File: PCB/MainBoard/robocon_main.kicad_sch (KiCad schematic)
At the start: 21 parts, among them J1 MOTOR_OUT, J10 Conn_01x03_Pin, J11 to_SERVO, J2 POWER, J3 MOTOR_OUT, J4 to_COLOR, J5 MOTOR_OUT, J7 MOTOR_OUT, J9 to_CAM, SW1 POW, U1 OKL-T/6-W12N-C, U2 RP2040, U3 TB67H450, U4 3-Terminal Regulator, U5 TB67H450, U6 TB67H450, U7 TB67H450, U8 BNO055

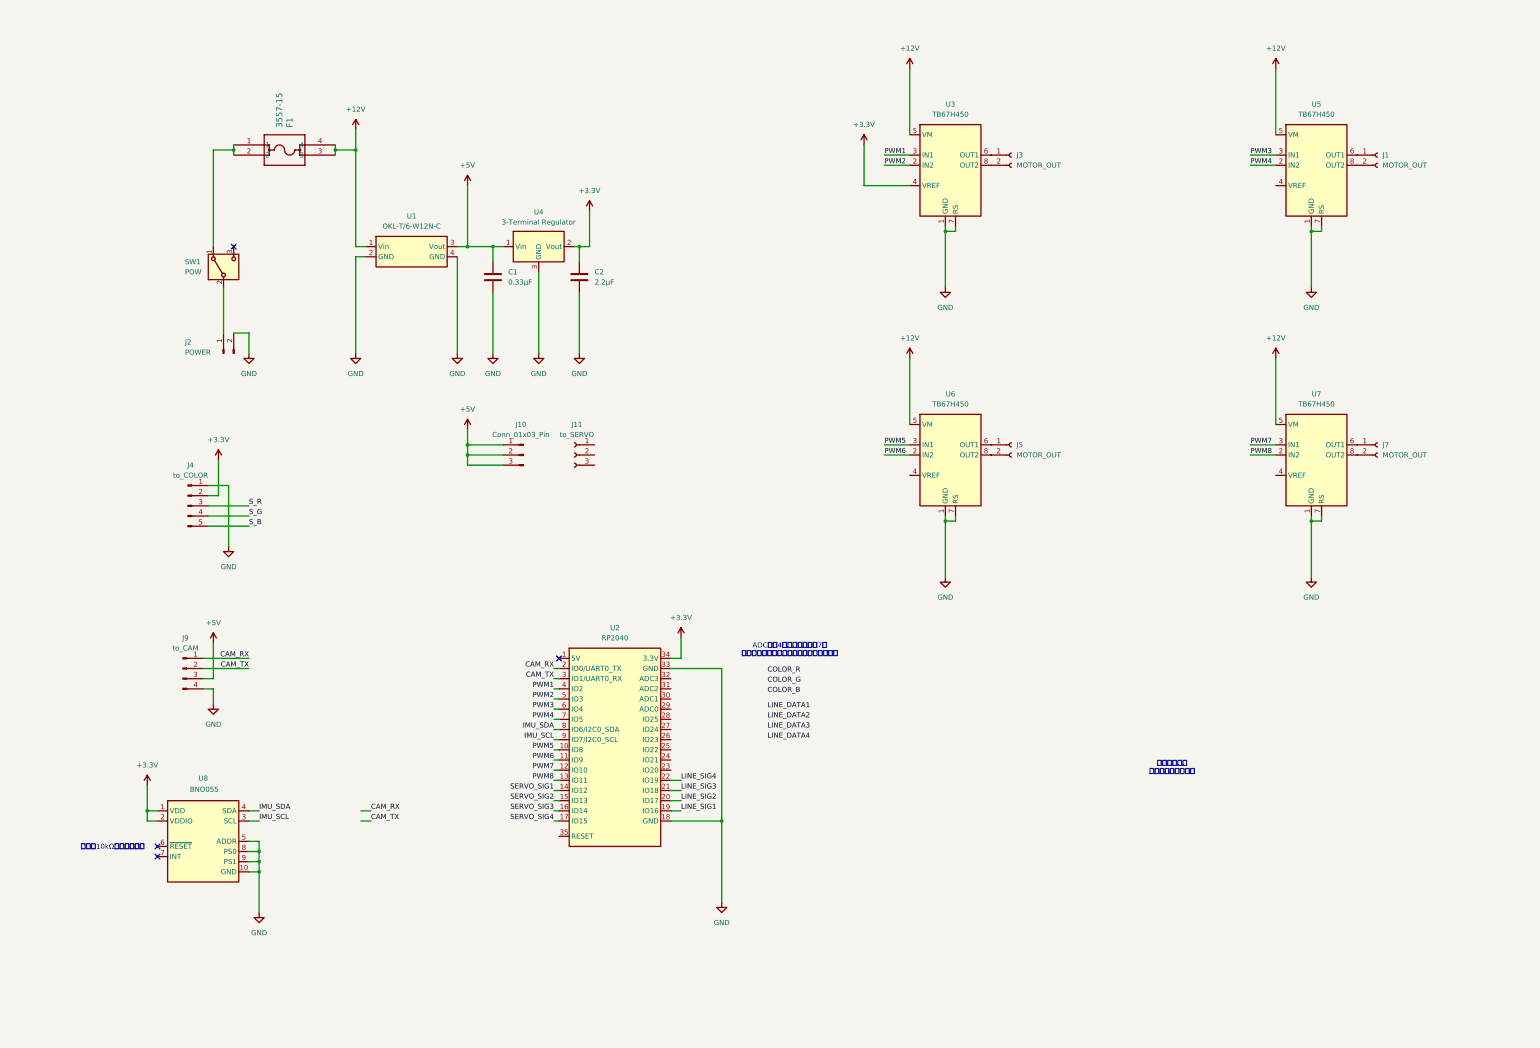
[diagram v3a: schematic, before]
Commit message: サーボ、ラインセンサのコネクタ化、ラベル更新
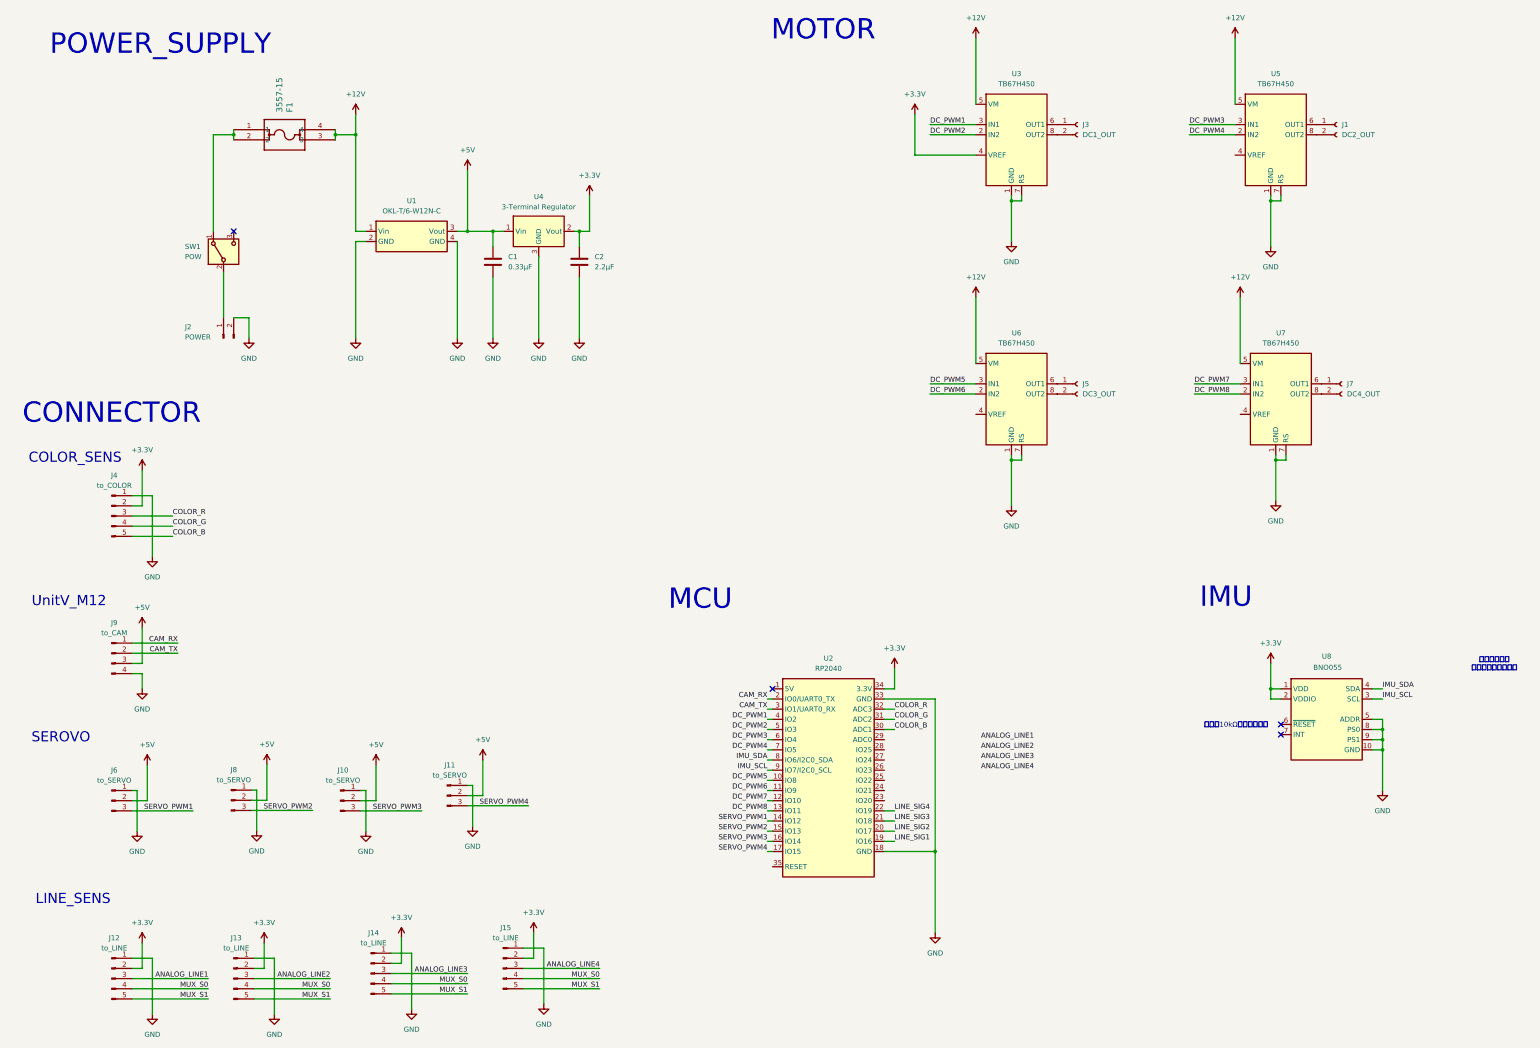
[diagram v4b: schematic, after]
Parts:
- removed J11: to_SERVO, symbol Connector:Conn_01x03_Socket
- added J11, J6, J8: to_SERVO, symbol Connector:Conn_01x03_Pin
- added J12, J13, J14, J15: to_LINE, symbol Connector:Conn_01x05_Pin
- J1: value MOTOR_OUT -> DC2_OUT
- J10: value Conn_01x03_Pin -> to_SERVO
- J3: value MOTOR_OUT -> DC1_OUT
- J5: value MOTOR_OUT -> DC3_OUT
- J7: value MOTOR_OUT -> DC4_OUT
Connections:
- net S_B is gone; now on net COLOR_B: J4.5 (Pin_5)
- net S_G is gone; now on net COLOR_G: J4.4 (Pin_4)
- net S_R is gone; now on net COLOR_R: J4.3 (Pin_3)
- net +3.3V: now also J12.2 (Pin_2), J13.2 (Pin_2), J14.2 (Pin_2), J15.2 (Pin_2)
- net +5V: now also J11.2 (Pin_2), J6.2 (Pin_2), J8.2 (Pin_2); no longer J10.1 (Pin_1), J10.3 (Pin_3)
- net COLOR_B: now also U2.30 (ADC1)
- net COLOR_G: now also U2.31 (ADC2)
- net COLOR_R: now also U2.32 (ADC3)
- net GND: now also J10.1 (Pin_1), J11.1 (Pin_1), J12.1 (Pin_1), J13.1 (Pin_1), J14.1 (Pin_1), J15.1 (Pin_1), J6.1 (Pin_1), J8.1 (Pin_1)
- net PWM1 renamed DC_PWM1
- net PWM2 renamed DC_PWM2
- net PWM3 renamed DC_PWM3
- net PWM4 renamed DC_PWM4
- net PWM5 renamed DC_PWM5
- net PWM6 renamed DC_PWM6
- net PWM7 renamed DC_PWM7
- net PWM8 renamed DC_PWM8
- net SERVO_SIG1 renamed SERVO_PWM1
- net SERVO_PWM1: now also J6.3 (Pin_3)
- net SERVO_SIG2 renamed SERVO_PWM2
- net SERVO_PWM2: now also J8.3 (Pin_3)
- net SERVO_SIG3 renamed SERVO_PWM3
- net SERVO_PWM3: now also J10.3 (Pin_3)
- net SERVO_SIG4 renamed SERVO_PWM4
- net SERVO_PWM4: now also J11.3 (Pin_3)
- new net ANALOG_LINE1: J12.3 (Pin_3)
- new net ANALOG_LINE2: J13.3 (Pin_3)
- new net ANALOG_LINE3: J14.3 (Pin_3)
- new net ANALOG_LINE4: J15.3 (Pin_3)
- new net MUX_S0: J12.4 (Pin_4), J13.4 (Pin_4), J14.4 (Pin_4), J15.4 (Pin_4)
- new net MUX_S1: J12.5 (Pin_5), J13.5 (Pin_5), J14.5 (Pin_5), J15.5 (Pin_5)
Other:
- note added: "COLOR_SENS"
- note added: "CONNECTOR"
- note added: "IMU"
- note added: "LINE_SENS"
- note added: "MCU"
- note added: "MOTOR"
- note added: "POWER_SUPPLY"
- note added: "SEROVO"
- note added: "UnitV_M12"
- note removed: "ADCピン4本に対して信号7本 どのようにつなぐ？（マルチプレクサ？）"
- moved on the sheet: C1, C2, F1, J1, J2, J3, J4, J5, J7, J9, SW1, U1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

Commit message: コネクタ、モタドラの修正 ＆ 電源周りのデバッグIF設計
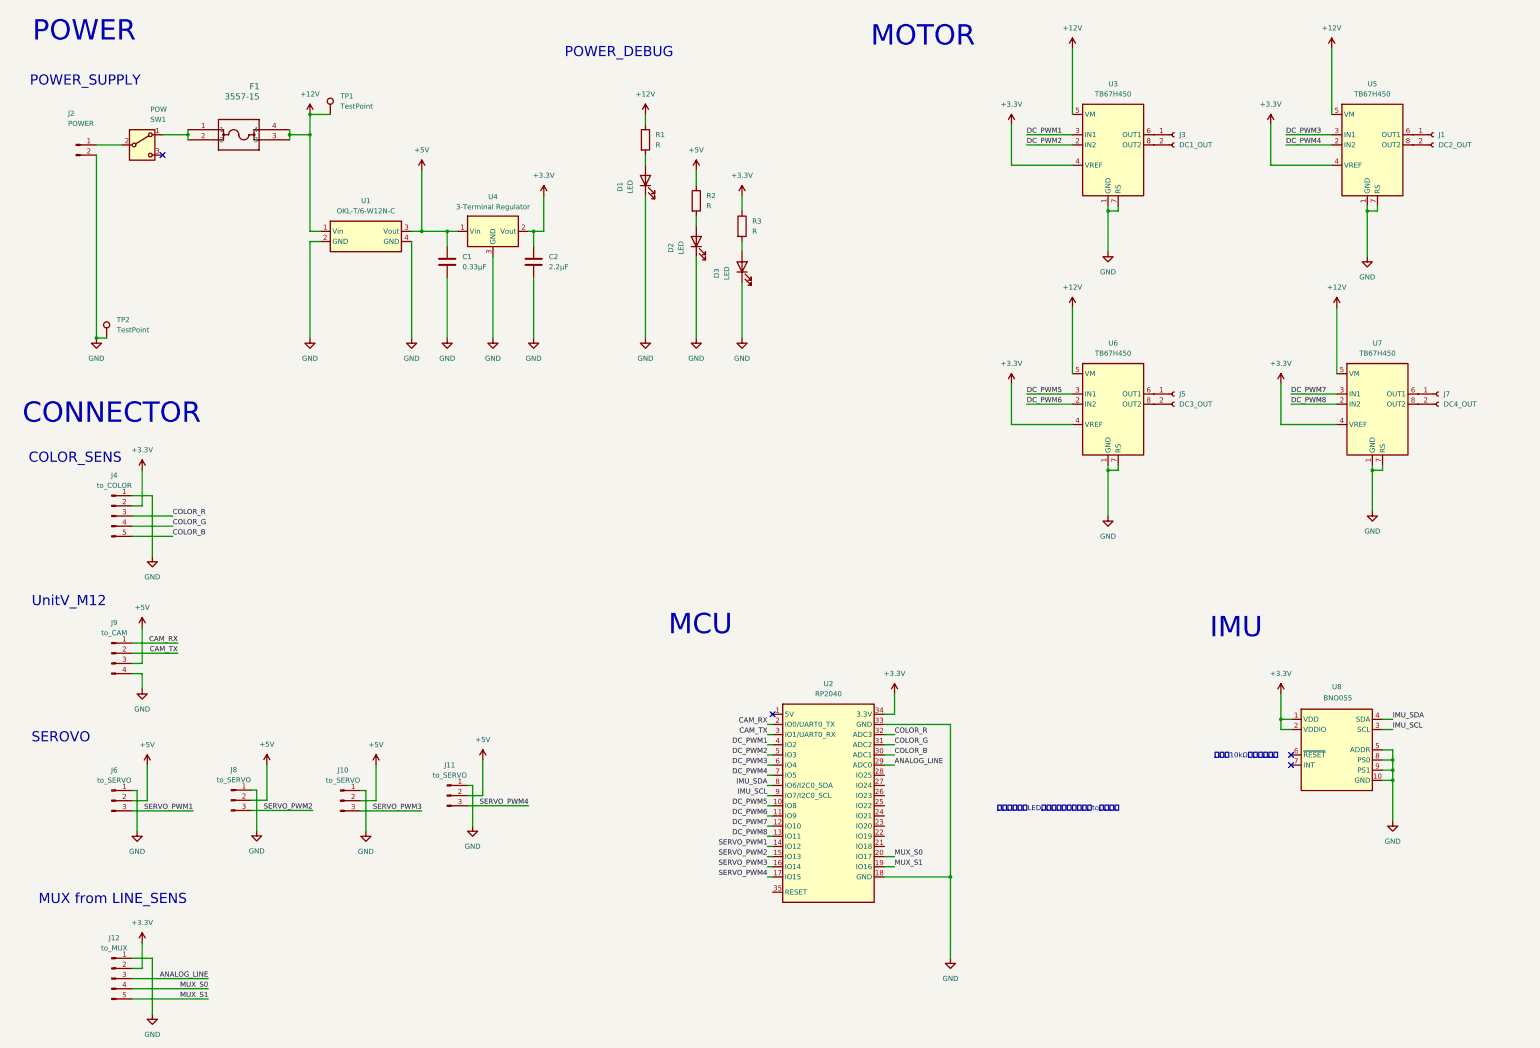
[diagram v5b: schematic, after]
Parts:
- removed J13, J14, J15: to_LINE, symbol Connector:Conn_01x05_Pin
- added D1, D2, D3: LED, symbol Device:LED
- added R1, R2, R3: R, symbol Device:R
- added TP1, TP2: TestPoint, symbol Connector:TestPoint
- J12: value to_LINE -> to_MUX
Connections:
- net ANALOG_LINE1 is gone; now on net ANALOG_LINE: J12.3 (Pin_3)
- net LINE_SIG1 is gone; now on net MUX_S1: U2.19 (IO16)
- net LINE_SIG2 is gone; now on net MUX_S0: U2.20 (IO17)
- net +12V: now also R1.1, TP1.1
- net +3.3V: now also U5.4 (VREF), U6.4 (VREF), U7.4 (VREF), R3.1
- net +5V: now also R2.1
- net GND: now also D1.1 (K), D2.1 (K), D3.1 (K), TP2.1
- net ANALOG_LINE: now reaches U2.29 (ADC0)
- net LINE_SIG3: no longer names the net of U2.21 (IO18)
- net LINE_SIG4: no longer names the net of U2.22 (IO19)
- new net: D2.2 (A), R2.2
- new net: D1.2 (A), R1.2
- new net: D3.2 (A), R3.2
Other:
- note added: "MUX from LINE_SENS"
- note added: "POWER"
- note added: "POWER_DEBUG"
- note added: "デバッグ用のLEDどれくらいほしい？（toソフト）"
- note removed: "LINE_SENS"
- note removed: "サーボのピン バイパスコンデンサ"
- moved on the sheet: C1, C2, F1, J1, J2, J3, J5, J7, SW1, U1, U2, U3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

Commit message: コネクタ追加
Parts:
- added J13: to_MD1, symbol Connector:Conn_01x02_Pin
- added J14: to_MD3, symbol Connector:Conn_01x02_Pin
- added J15: to_MD2, symbol Connector:Conn_01x02_Pin
- added J16: to_MD4, symbol Connector:Conn_01x02_Pin
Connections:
- net DC_PWM1: now also J13.1 (Pin_1)
- net DC_PWM2: now also J13.2 (Pin_2)
- net DC_PWM3: now also J15.1 (Pin_1)
- net DC_PWM4: now also J15.2 (Pin_2)
- net DC_PWM5: now also J14.1 (Pin_1)
- net DC_PWM6: now also J14.2 (Pin_2)
- net DC_PWM7: now also J16.1 (Pin_1)
- net DC_PWM8: now also J16.2 (Pin_2)
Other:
- note added: "MOTOR_DRIVER"

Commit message: フットプリント割り当て_ver.1
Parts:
- F1: footprint 3557-15_KEY -> my_footprints_library:3557-15_KEY
- J10: value to_SERVO -> to_SERVO3; footprint (none) -> Connector_PinHeader_2.54mm:PinHeader_1x03_P2.54mm_Vertical
- J11: value to_SERVO -> to_SERVO4; footprint (none) -> Connector_PinHeader_2.54mm:PinHeader_1x03_P2.54mm_Vertical
- J12: footprint (none) -> Connector_JST:JST_PH_B5B-PH-K_1x05_P2.00mm_Vertical
- J13, J14, J15, J16: footprint (none) -> Connector_JST:JST_XA_B02B-XASK-1-A_1x02_P2.50mm_Vertical
- J2: footprint (none) -> Connector_AMASS:AMASS_XT30U-M_1x02_P5.0mm_Vertical
- J6: value to_SERVO -> to_SERVO1; footprint (none) -> Connector_PinHeader_2.54mm:PinHeader_1x03_P2.54mm_Vertical
- J7: footprint (none) -> Connector_PinHeader_2.54mm:PinHeader_1x03_P2.54mm_Vertical
- J8: value to_SERVO -> to_SERVO2; footprint (none) -> Connector_PinHeader_2.54mm:PinHeader_1x03_P2.54mm_Vertical
- J9: footprint (none) -> Connector:NS-Tech_Grove_1x04_P2mm_Vertical
- TP1, TP2: footprint (none) -> TestPoint:TestPoint_Pad_2.0x2.0mm
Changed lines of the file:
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@@
 			)
 		)
-		(property "Footprint" ""
+		(property "Footprint" "Connector_AMASS:AMASS_XT30U-M_1x02_P5.0mm_Vertical"
 			(at 29.21 49.53 0)
 			(effects
@@
 			)
 		)
-		(property "Footprint" ""
+		(property "Footprint" "Connector_JST:JST_PH_B5B-PH-K_1x05_P2.00mm_Vertical"
 			(at 38.1 257.81 0)
 			(effects
@@
 			)
 		)
-		(property "Footprint" ""
+		(property "Footprint" "Connector_JST:JST_XA_B02B-XASK-1-A_1x02_P2.50mm_Vertical"
 			(at 160.02 134.62 0)
 			(effects
@@
 			)
 		)
-		(property "Value" "to_SERVO"
+		(property "Value" "to_SERVO3"
 			(at 95.885 208.28 0)
 			(effects
@@
 			)
 		)
-		(property "Footprint" ""
+		(property "Footprint" "Connector_PinHeader_2.54mm:PinHeader_1x03_P2.54mm_Vertical"
 			(at 95.25 213.36 0)
 			(effects
@@
 			)
 		)
-		(property "Value" "to_SERVO"
+		(property "Value" "to_SERVO1"
 			(at 38.735 208.28 0)
 			(effects
@@
 			)
 		)
-		(property "Footprint" ""
+		(property "Footprint" "Connector_PinHeader_2.54mm:PinHeader_1x03_P2.54mm_Vertical"
 			(at 38.1 213.36 0)
 			(effects
@@
 			)
 		)
-		(property "Footprint" ""
+		(property "Footprint" "Connector_PinHeader_2.54mm:PinHeader_1x03_P2.54mm_Vertical"
 			(at 369.57 111.76 0)
 			(effects
@@
 			)
 		)
-		(property "Footprint" ""
+		(property "Footprint" "TestPoint:TestPoint_Pad_2.0x2.0mm"
 			(at 87.63 41.91 0)
 			(effects
@@
 			)
 		)
-		(property "Footprint" "3557-15_KEY"
+		(property "Footprint" "my_footprints_library:3557-15_KEY"
 			(at 57.15 45.72 0)
 			(effects
@@
 			)
 		)
-		(property "Footprint" ""
+		(property "Footprint" "TestPoint:TestPoint_Pad_2.0x2.0mm"
 			(at 41.91 97.79 0)
 			(effects
@@
 			)
 		)
-		(property "Footprint" ""
+		(property "Footprint" "Connector_JST:JST_XA_B02B-XASK-1-A_1x02_P2.50mm_Vertical"
 			(at 130.81 134.62 0)
 			(effects
@@
 			)
 		)
-		(property "Footprint" ""
+		(property "Footprint" "Connector:NS-Tech_Grove_1x04_P2mm_Vertical"
 			(at 38.1 176.53 0)
 			(effects
@@
 			)
 		)
-		(property "Footprint" ""
+		(property "Footprint" "Connector_JST:JST_XA_B02B-XASK-1-A_1x02_P2.50mm_Vertical"
 			(at 99.06 134.62 0)
 			(effects
@@
 		(fields_autoplaced yes)
 		(property "Reference" "J8"
-			(at 68.6046 205.6412 0)
+			(at 68.6046 205.74 0)
 			(effects
 				(font
@@
 			)
 		)
-		(property "Value" "to_SERVO"
-			(at 68.6046 208.1812 0)
+		(property "Value" "to_SERVO2"
+			(at 68.6046 208.28 0)
 			(effects
 				(font
@@
 			)
 		)
-		(property "Footprint" ""
+		(property "Footprint" "Connector_PinHeader_2.54mm:PinHeader_1x03_P2.54mm_Vertical"
 			(at 67.9696 213.2612 0)
 			(effects
@@
 			)
 		)
-		(property "Value" "to_SERVO"
+		(property "Value" "to_SERVO4"
 			(at 122.555 207.01 0)
 			(effects
@@
 			)
 		)
-		(property "Footprint" ""
+		(property "Footprint" "Connector_PinHeader_2.54mm:PinHeader_1x03_P2.54mm_Vertical"
 			(at 121.92 212.09 0)
 			(effects
@@
 			)
 		)
-		(property "Footprint" ""
+		(property "Footprint" "Connector_JST:JST_XA_B02B-XASK-1-A_1x02_P2.50mm_Vertical"
 			(at 191.77 134.62 0)
 			(effects

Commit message: 発注用データ
GitHubデスクトップ直った！
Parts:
- removed J10: to_SERVO3, Connector_PinHeader_2.54mm:PinHeader_1x03_P2.54mm_Vertical, symbol Connector:Conn_01x03_Pin
- removed J11: to_SERVO4, Connector_PinHeader_2.54mm:PinHeader_1x03_P2.54mm_Vertical, symbol Connector:Conn_01x03_Pin
- removed J15: to_MD2, Connector_JST:JST_XA_B02B-XASK-1-A_1x02_P2.50mm_Vertical, symbol Connector:Conn_01x02_Pin
- removed J16: to_MD4, Connector_JST:JST_XA_B02B-XASK-1-A_1x02_P2.50mm_Vertical, symbol Connector:Conn_01x02_Pin
- removed U1: OKL-T/6-W12N-C, symbol my_symbol:OKL-T/6-W12N-C
- added C3: 10μF, Capacitor_SMD:C_1206_3216Metric_Pad1.33x1.80mm_HandSolder, symbol Device:C
- added D4, D5, D6, D7: LED, LED_SMD:LED_0603_1608Metric_Pad1.05x0.95mm_HandSolder, symbol Device:LED
- added D8, D9: D, my_footprints_library:MA10EB045, symbol Device:D
- added J15: Conn_01x02_Pin, Connector_JST:JST_PH_B6B-PH-K_1x06_P2.00mm_Vertical, symbol Connector:Conn_01x06_Pin
- added R4, R5, R6, R7, R8, R9: R, Resistor_SMD:R_0603_1608Metric_Pad0.98x0.95mm_HandSolder, symbol Device:R
- added SW2, SW3: SW_Push, Button_Switch_THT:SW_PUSH_6mm_H7.3mm, symbol Switch:SW_Push
- C1, C2: footprint (none) -> Capacitor_SMD:C_0603_1608Metric_Pad1.08x0.95mm_HandSolder
- D1, D2, D3: footprint (none) -> LED_SMD:LED_0603_1608Metric_Pad1.05x0.95mm_HandSolder
- J1, J3, J5: footprint (none) -> Connector_JST:JST_XA_B02B-XASK-1-A_1x02_P2.50mm_Vertical
- J13: value to_MD1 -> to_OKL-T/6-W12N-C; footprint Connector_JST:JST_XA_B02B-XASK-1-A_1x02_P2.50mm_Vertical -> Connector_Wire:SolderWirePad_1x01_SMD_3x6mm
- J14: value to_MD3 -> from_OKL-T/6-W12N-C; footprint Connector_JST:JST_XA_B02B-XASK-1-A_1x02_P2.50mm_Vertical -> Connector_Wire:SolderWirePad_1x01_SMD_3x6mm
- J7: footprint Connector_PinHeader_2.54mm:PinHeader_1x03_P2.54mm_Vertical -> Connector_JST:JST_XA_B02B-XASK-1-A_1x02_P2.50mm_Vertical
- R1, R2, R3: footprint (none) -> Resistor_SMD:R_0603_1608Metric_Pad0.98x0.95mm_HandSolder
- SW1: footprint (none) -> my_footprints_library:1P2T_toggle
- U4: footprint (none) -> Package_TO_SOT_SMD:TO-252-3_TabPin2
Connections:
- net +12V: now also J13.1 (Pin_1), SW1.1 (A), C3.2, D8.1 (K), J15.2 (Pin_2); no longer F1.3, F1.4
- net +3.3V: now also D9.2 (A), R8.1, R9.1
- net +5V: now also J14.1 (Pin_1), D8.2 (A), D9.1 (K)
- net DC_PWM1: no longer J13.1 (Pin_1)
- net DC_PWM2: no longer J13.2 (Pin_2)
- net DC_PWM5: no longer J14.1 (Pin_1)
- net DC_PWM6: no longer J14.2 (Pin_2)
- net GND: now also J13.2 (Pin_2), J14.2 (Pin_2), J2.1 (Pin_1), C3.1, D4.1 (K), D5.1 (K), D6.1 (K), D7.1 (K), J15.1 (Pin_1), SW2.2, SW3.2; no longer J2.2 (Pin_2)
- net SERVO_PWM1: now also U2.21 (IO18); no longer U2.14 (IO12)
- net SERVO_PWM2: now also U2.22 (IO19); no longer U2.15 (IO13)
- net at F1.1, F1.2: now also J2.2 (Pin_2); no longer SW1.1 (A)
- net at SW1.2 (B): now also F1.3, F1.4; no longer J2.1 (Pin_1)
- net TACT_SW1: now reaches U2.23 (IO20)
- net TACT_SW1: now also R8.2, SW2.1
- net TACT_SW2: now reaches U2.24 (IO21)
- net TACT_SW2: now also R9.2, SW3.1
- net NchFET_3: now reaches U2.25 (IO22)
- net NchFET_3: now also J15.6 (Pin_6)
- net NchFET_2: now reaches U2.26 (IO23)
- net NchFET_2: now also J15.5 (Pin_5)
- net NchFET_1: now reaches U2.27 (IO24)
- net NchFET_1: now also J15.4 (Pin_4)
- net PchFET: now reaches U2.28 (IO25)
- net PchFET: now also J15.3 (Pin_3)
- net SERVO_PWM3 renamed DEBUG_LED3
- net DEBUG_LED3: now also R6.1
- net SERVO_PWM4 renamed DEBUG_LED4
- net DEBUG_LED4: now also R7.1
- new net: D7.2 (A), R7.2
- new net: D6.2 (A), R6.2
- new net: D5.2 (A), R5.2
- new net: D4.2 (A), R4.2
- new net DEBUG_LED1: R4.1, U2.14 (IO12)
- new net DEBUG_LED2: R5.1, U2.15 (IO13)
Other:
- note added: "Rいる？？？→ センサ、マイコンでの消費電流が変動 するのでここにかかる電力が未確定 →抵抗が耐えられないかも？ →慎重に検討 →コンデンサのみで十分"
- note added: "SOLENOID"
- note removed: "MOTOR_DRIVER"
- note removed: "デバッグ用のLEDどれくらいほしい？（toソフト）"
- moved on the sheet: C1, C2, D1, D2, D3, F1, J1, J2, J3, J5, J7, R1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
